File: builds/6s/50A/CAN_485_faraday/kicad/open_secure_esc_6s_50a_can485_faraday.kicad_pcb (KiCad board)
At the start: 4 copper layers, 32 x 66.1 mm, 59 parts, among them J1 SolderPad_1x04_SMD_P1.27mm_Pr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, J2 SolderPad_1x02_SMD_P2.54mm, J3 SolderPad_1x02_SMD_P2.54mm, J4A SolderWirePad_1x01_SMD_5x10mm, J4B SolderWirePad_1x01_SMD_5x10mm, J4C SolderWirePad_1x01_SMD_5x10mm, J5A SolderWire-6sqmm_1x01_D3.5mm_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, J5B SolderWire-6sqmm_1x01_D3.5mm_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, Q1 Toshiba_2-5W1A_SOP-Advance-N_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, Q2 Toshiba_2-5W1A_SOP-Advance-N_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, Q3 Toshiba_2-5W1A_SOP-Advance-N_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, Q4 Toshiba_2-5W1A_SOP-Advance-N_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, Q5 Toshiba_2-5W1A_SOP-Advance-N_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, Q6 Toshiba_2-5W1A_SOP-Advance-N_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, U1 LQFP-64_10x10mm_P0.5mm, U2 Infineon_PG-USON-10-2-4_3x3mm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, U3 SOIC-20W_7.5x12.8mm_P1.27mm, U4 SOIC-20W_7.5x12.8mm_P1.27mm, U5 TI_RTA0040B_WQFN-40_6x6mm_P0.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, U6 SOIC-8_3.9x4.9mm_P1.27mm, U7 SOIC-8_3.9x4.9mm_P1.27mm, U8 SOIC-8_3.9x4.9mm_P1.27mm

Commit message: PROJECT_INDEX: list the clean-build tools and score_placement
Adds the four tools from the clean-build pass plus score_placement.py, which
predates this pass but was never indexed.

Co-Authored-By: Claude Opus 5 <noreply@anthropic.com>
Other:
- board text added: "Open Secure ESC 50A 6S Shielded CAN + RS485 Griffing Technology LLC CERN-OHL-P 2.0 2026"
- board text removed: "Open Secure ESC 50A 6S Shielded CAN + RS485 Griffing Tech LLC CERN-OHL-P 2.0 2026"
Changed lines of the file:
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@@
 		(layer "Edge.Cuts")
 	)
-	(gr_text "Open Secure ESC\n50A 6S Shielded CAN + RS485\nGriffing Tech LLC \nCERN-OHL-P 2.0  2026\n"
+	(gr_text "Open Secure ESC\n50A 6S Shielded CAN + RS485\nGriffing Technology LLC \nCERN-OHL-P 2.0  2026\n"
 		(at 36.5 40 0)
 		(layer "F.SilkS")

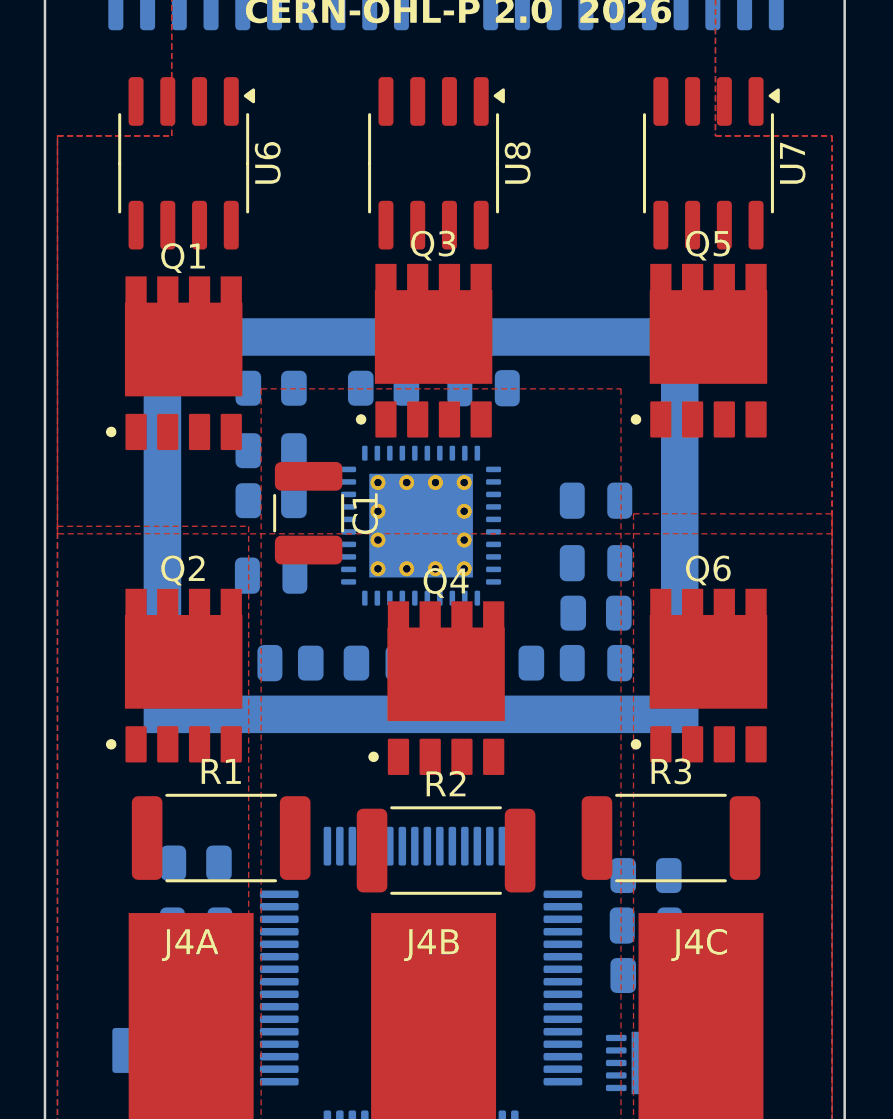
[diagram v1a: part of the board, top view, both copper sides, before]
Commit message: Restore the island + silk fixes a concurrent KiCad save reverted
CORRECTION TO e7c5171. That commit's message claims "78 -> 16 DRC violations,
zero errors remaining". The measurement was real, but the file it describes is
not the file it committed. Running DRC on e7c5171's own blob gives 56
violations, not 16. 4ba392b carried the same regression forward.

What happened: the repo owner had the board open in KiCad during the
clean-build pass and saved it. KiCad wrote its in-memory copy, which had been
loaded during the window when remove_vm_island.py had crashed on an LSET
constructor and not yet been re-run -- so that save carried the via and
thermal fixes but predated the island rule area and all 30 silkscreen moves.
My `git add -A` then committed the reverted board without noticing, because I
verified the numbers before the save and never re-read the file after it.

Two lessons, both mine: `git add -A` after a long tool sequence commits
whatever is on disk now, not what was measured earlier; and a clean
`git status` means the working tree matches HEAD, which is not the same as
"nobody else changed anything" -- here it meant the opposite.

Restored: remove_vm_island.py and tidy_silkscreen.py re-run, zones refilled.
Back to 16 violations, all warning severity, unconnected 158, creepage
7.83 mm, both isolation rules PASS.

THE REPO OWNER'S TWO CHANGES ARE PRESERVED, and both are good:

  * Silk attribution label (F.Silkscreen, x 4.50..28.70, y 13.67..20.37
    board-local) -- "Open Secure ESC / 50A 6S Shielded CAN + RS485 /
    Griffing Technology LLC / CERN-OHL-P 2.0 2026". Sits in the clear band
    between the J5 pack terminals (end y 13.12) and the U6/U8/U7 row (starts
    y 21.88): 0.55 mm above, 1.51 mm below. 1.00 mm text height against a
    0.8 mm minimum, 0.200 mm thickness against 0.08. Adds no violation, and
    tidy_silkscreen.py treats it as an obstacle so designators route around
    it rather than into it.

  * J5B moved y 28.8 -> 29.0, aligning it wit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
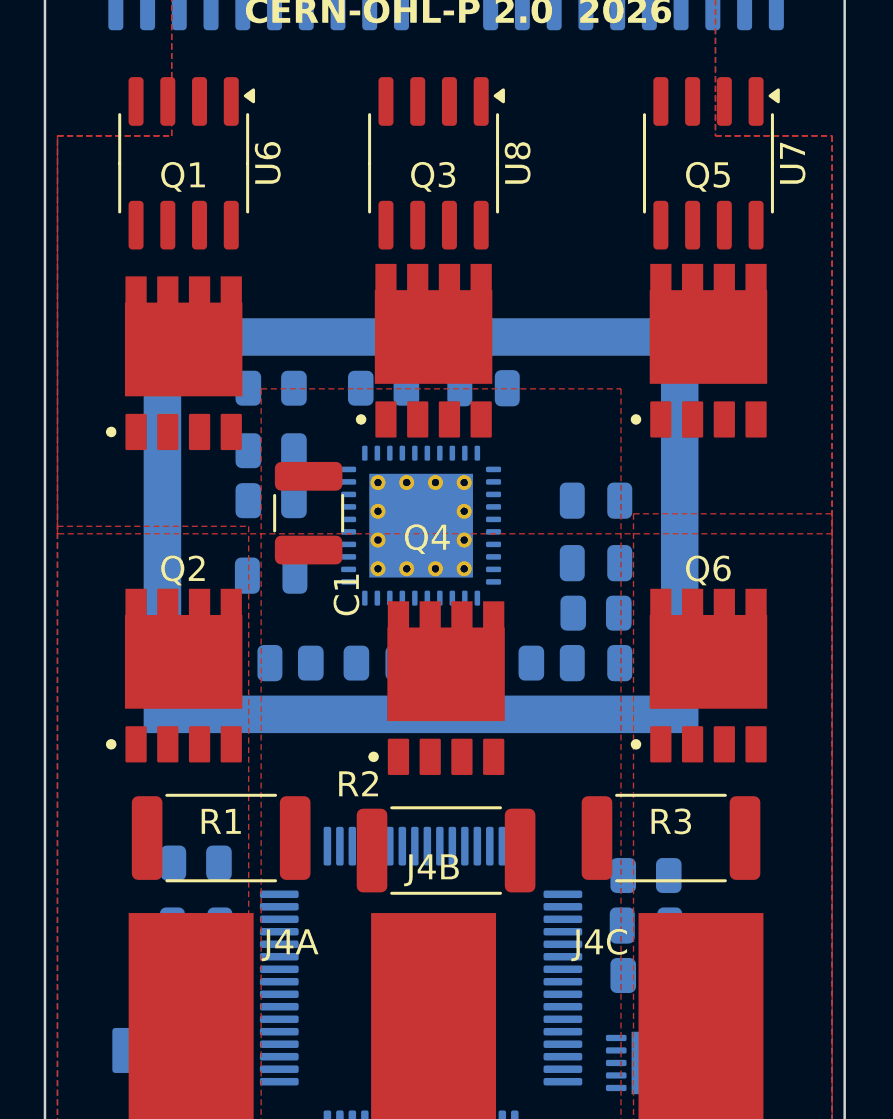
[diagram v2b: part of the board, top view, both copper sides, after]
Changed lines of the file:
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@@
 		(tags "resistor")
 		(property "Reference" "R1"
-			(at 0 -2.63 0)
+			(at 0 -0.63 0)
 			(layer "F.SilkS")
 			(effects
@@
 		(tags "resistor")
 		(property "Reference" "R3"
-			(at 0 -2.63 0)
+			(at 0 -0.63 0)
 			(layer "F.SilkS")
 			(effects
@@
 		(tags "MesurementPoint Square SMDPad 5mmx10mm ")
 		(property "Reference" "J4C"
-			(at 0 -3.81 0)
+			(at -4 -3.81 0)
 			(layer "F.SilkS")
 			(effects
@@
 		(tags "Toshiba 2-5W1A SOP Advance N MOSFET TPHR8504PL power 5x6")
 		(property "Reference" "Q1"
-			(at 0 -4.25 0)
+			(at 0 -7.5 0)
 			(layer "F.SilkS")
 			(effects
@@
 		(tags "MesurementPoint Square SMDPad 5mmx10mm ")
 		(property "Reference" "J4B"
-			(at 0 -3.81 0)
+			(at 0 -6.81 0)
 			(layer "F.SilkS")
 			(effects
@@
 		(tags "MesurementPoint Square SMDPad 5mmx10mm ")
 		(property "Reference" "J4A"
-			(at 0 -3.81 0)
+			(at 4 -3.81 0)
 			(layer "F.SilkS")
 			(effects
@@
 		(tags "Toshiba 2-5W1A SOP Advance N MOSFET TPHR8504PL power 5x6")
 		(property "Reference" "Q5"
-			(at 0 -4.25 0)
+			(at 0 -7 0)
 			(layer "F.SilkS")
 			(effects
@@
 		(tags "resistor")
 		(property "Reference" "R2"
-			(at 0 -2.63 0)
+			(at -3.5 -2.63 0)
 			(layer "F.SilkS")
 			(effects
@@
 		(tags "Toshiba 2-5W1A SOP Advance N MOSFET TPHR8504PL power 5x6")
 		(property "Reference" "Q3"
-			(at 0 -4.25 0)
+			(at 0 -7 0)
 			(layer "F.SilkS")
 			(effects
@@
 		(tags "Toshiba 2-5W1A SOP Advance N MOSFET TPHR8504PL power 5x6")
 		(property "Reference" "Q4"
-			(at 0 -4.25 0)
+			(at -0.75 -6 0)
 			(layer "F.SilkS")
 			(effects
@@
 		(tags "capacitor")
 		(property "Reference" "C1"
-			(at 0 -2.3 90)
+			(at 3.25 -1.55 90)
 			(layer "F.SilkS")
 			(effects
@@
 		(tags "capacitor")
 		(property "Reference" "C10"
-			(at 0 1.68 0)
+			(at 3.25 1.68 0)
 			(layer "B.SilkS")
 			(effects
@@
 		(tags "resistor")
 		(property "Reference" "R6"
-			(at 0 1.65 0)
+			(at 1.25 3.9 0)
 			(layer "B.SilkS")
 			(effects
@@
 		(tags "capacitor")
 		(property "Reference" "C11"
-			(at 0 1.68 0)
+			(at 3.25 1.68 0)
 			(layer "B.SilkS")
 			(effects
@@
 		(tags "inductor")
 		(property "Reference" "FB3"
-			(at 0 1.17 0)
+			(at -3.25 1.17 0)
 			(layer "B.SilkS")
 			(effects
@@
 		(tags "resistor")
 		(property "Reference" "R9"
-			(at 0 1.65 0)
+			(at 0 3.9 0)
 			(layer "B.SilkS")
 			(effects
@@
 		(tags "capacitor")
 		(property "Reference" "C2"
-			(at 0 1.68 0)
+			(at -0.25 3.93 0)
 			(layer "B.SilkS")
 			(effects
@@
 		(tags "solder pad SMD wire connector 1x02 2.54mm")
 		(property "Reference" "J2"
-			(at 0 2.6 0)
+			(at 0 5.35 0)
 			(layer "B.SilkS")
 			(effects
@@
 		(tags "capacitor")
 		(property "Reference" "C3"
-			(at 0 1.68 0)
+			(at 2.75 1.68 0)
 			(layer "B.SilkS")
 			(effects
@@
 		(tags "capacitor")
 		(property "Reference" "C6"
-			(at 0 1.68 0)
+			(at 2.25 4.18 0)
 			(layer "B.SilkS")
 			(effects
@@
 		(tags "capacitor")
 		(property "Reference" "C15"
-			(at 0 1.68 0)
+			(at -3.25 -0.07 0)
 			(layer "B.SilkS")
 			(effects
@@
 		(tags "resistor")
 		(property "Reference" "R12"
-			(at 0 1.65 0)
+			(at 3.25 1.65 0)
 			(layer "B.SilkS")
 			(effects
@@
 		(tags "inductor")
 		(property "Reference" "FB2"
-			(at 0 1.17 180)
+			(at -0.25 -1.33 180)
 			(layer "B.SilkS")
 			(effects
@@
 		(tags "capacitor")
 		(property "Reference" "C12"
-			(at 0 1.68 0)
+			(at 3.25 1.68 0)
 			(layer "B.SilkS")
 			(effects
@@
 		(tags "resistor")
 		(property "Reference" "R8"
-			(at 0 1.65 0)
+			(at -2.75 4.15 0)
 			(layer "B.SilkS")
 			(effects
@@
 		(tags "inductor")
 		(property "Reference" "FB4"
-			(at 0 1.17 180)
+			(at 0.75 -1.33 180)
 			(layer "B.SilkS")
 			(effects
@@
 		(tags "solder pad SMD wire connector 1x02 2.54mm")
 		(property "Reference" "J3"
-			(at 0 2.6 180)
+			(at 0 5.35 180)
 			(layer "B.SilkS")
 			(effects
@@
 		(tags "capacitor")
 		(property "Reference" "C16"
-			(at 0 1.68 0)
+			(at 0 3.68 0)
 			(layer "B.SilkS")
 			(effects
@@
 		(tags "capacitor")
 		(property "Reference" "C4"
-			(at 0 1.68 0)
+			(at 2.75 1.68 0)
 			(layer "B.SilkS")
 			(effects
@@
 		(tags "USON DFN PG-USON-10 OPTIGA TrustM Infineon SMD thermal-pad")
 		(property "Reference" "U2"
-			(at 0 2.5 0)
+			(at -3.5 2 0)
 			(layer "B.SilkS")
 			(effects
@@
 			)
 		)
+	)
+	(zone
+		(net 0)
+		(net_name "")
+		(layer "In2.Cu")
+		(name "VM island under U5 via ring")
+		(hatch edge 0.5)
+		(connect_pads
+			(clearance 0)
+		)
+		(min_thickness 0.25)
+		(filled_areas_thickness no)
+		(keepout
+			(tracks allowed)
+			(vias allowed)
+			(pads allowed)
+			(copperpour not_allowed)
+			(footprints allowed)
+		)
+		(placement
+			(enabled no)
+			(sheetname "")
+		)
+		(fill
+			(thermal_gap 0.5)
+			(thermal_bridge_width 0.5)
+		)
+		(polygon
+			(pts
+				(xy 33.45 58.45) (xy 36.549999 58.45) (xy 36.549999 60.65) (xy 33.45 60.65)
+			)
+		)

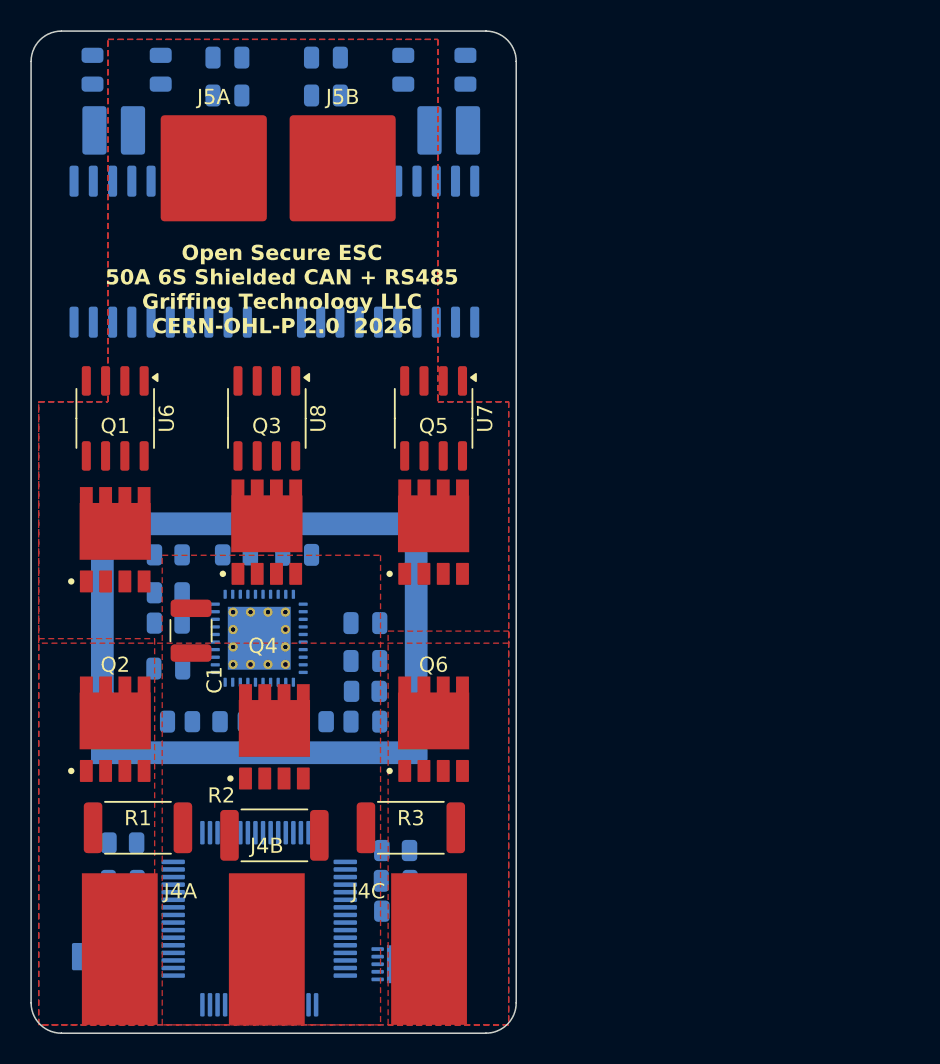
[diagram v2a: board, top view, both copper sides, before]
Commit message: Align, centre and symmetrize the layout; put U7/U8 on their own phases
All geometry work is measured, and every move is reverted unless the harness
says it cost nothing: DRC electrical 0, unconnected not rising, creepage not
falling, isolated lead within 10.0 mm, gate and commutation loops not growing,
both isolation rules still passing.

RESULT
    phase pitch          10.500 / 10.500 mm  (was 10.000 / 11.000)
    phase B              exactly on the centreline x = 16.000
    mirror pairs         12 / 12 symmetric
    off the 0.5 mm grid  0 parts in x
    creepage             7.83 mm   unchanged
    isolated lead        9.92 -> 9.76 mm   improved
    commutation loop     19.60 -> 19.40 mm   improved
    gate loop            16.49 -> 16.53 mm   +0.04, within tolerance
    unconnected          158 -> 157
    DRC                  16 violations, all warning severity

THE CENTRELINE IS 16.000, NOT 16.050. GetBoardEdgesBoundingBox() reports
32.100 mm because it measures the outer extent of the 0.05 mm Edge.Cuts
stroke. The true outline is 32.000. Using the bounding box would have pushed
every symmetric pair 0.05 mm off-grid -- the same 0.05 mm that once put pads
0.02 mm short of the edge rule on this board.

THE MAJORITY ROW IS NOT AUTOMATICALLY THE RIGHT ROW. align_rows_columns.py
first snapped outliers to the position most of their group shared. On the
high-side FETs that moved Q1 up to Q3/Q5, pulling it away from U5 and
lengthening the worst gate loop 16.49 -> 16.74, so the guard reverted it and
the row stayed crooked. The correct move was the opposite: bring Q3 and Q5
DOWN to Q1, which aligns all six FETs and shortens the commutation loop,
because it moves two parts toward the driver instead of one away. The tool now
scores every distinct position a group occupies.

SYMMETRY AND GRID CONFLICT unless a pair's separation is a whole millimetre --
centring splits it in half, so 8.500 apart becomes +/-4.250. Centring alone
dropped grid adherence 83.1% -> 44.1%. Resolved by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
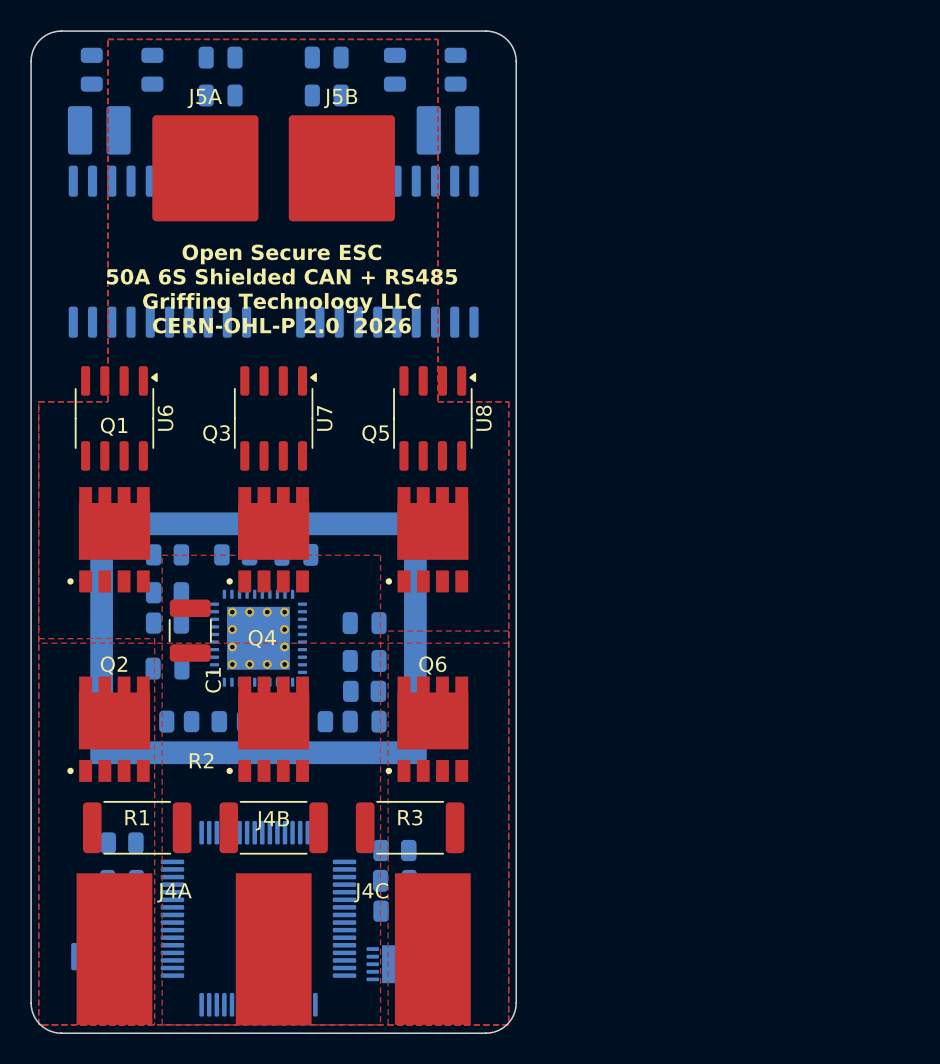
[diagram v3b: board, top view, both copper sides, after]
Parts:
- moved U8 10.9 mm to (46.4, 45.5)
- moved U7 10.6 mm to (35.9, 45.5)
- moved J2 0.95 mm to (24.4, 26.5)
- moved Q3 0.67 mm to (35.9, 53.5)
- moved C18 0.65 mm to (47.9, 22.5)
- moved C13 0.55 mm to (27.9, 22.5)
- moved C17 0.55 mm to (43.9, 22.5)
- moved J5A 0.55 mm to (31.4, 29.0)
- moved Q4 0.50 mm to (35.9, 66.0)
- moved Q5 0.50 mm to (46.4, 53.5)
- moved R2 0.50 mm to (35.9, 72.5)
- moved C11 0.45 mm to (32.4, 21.7)
- moved C12 0.45 mm to (32.4, 24.2)
- moved J4B 0.45 mm to (35.9, 80.5)
- moved J4A 0.35 mm to (25.4, 80.5)
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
